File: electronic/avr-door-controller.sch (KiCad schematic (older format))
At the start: 74 parts, among them CON1 24V, J1 DOOR1, J2 DOOR2, P1 Digital, P10 DOOR2 BTN, P2 Analog, P3 DOOR1 BTN, P6 USB_A, P7 CLOCK, Q1 Q_NPN_EBC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

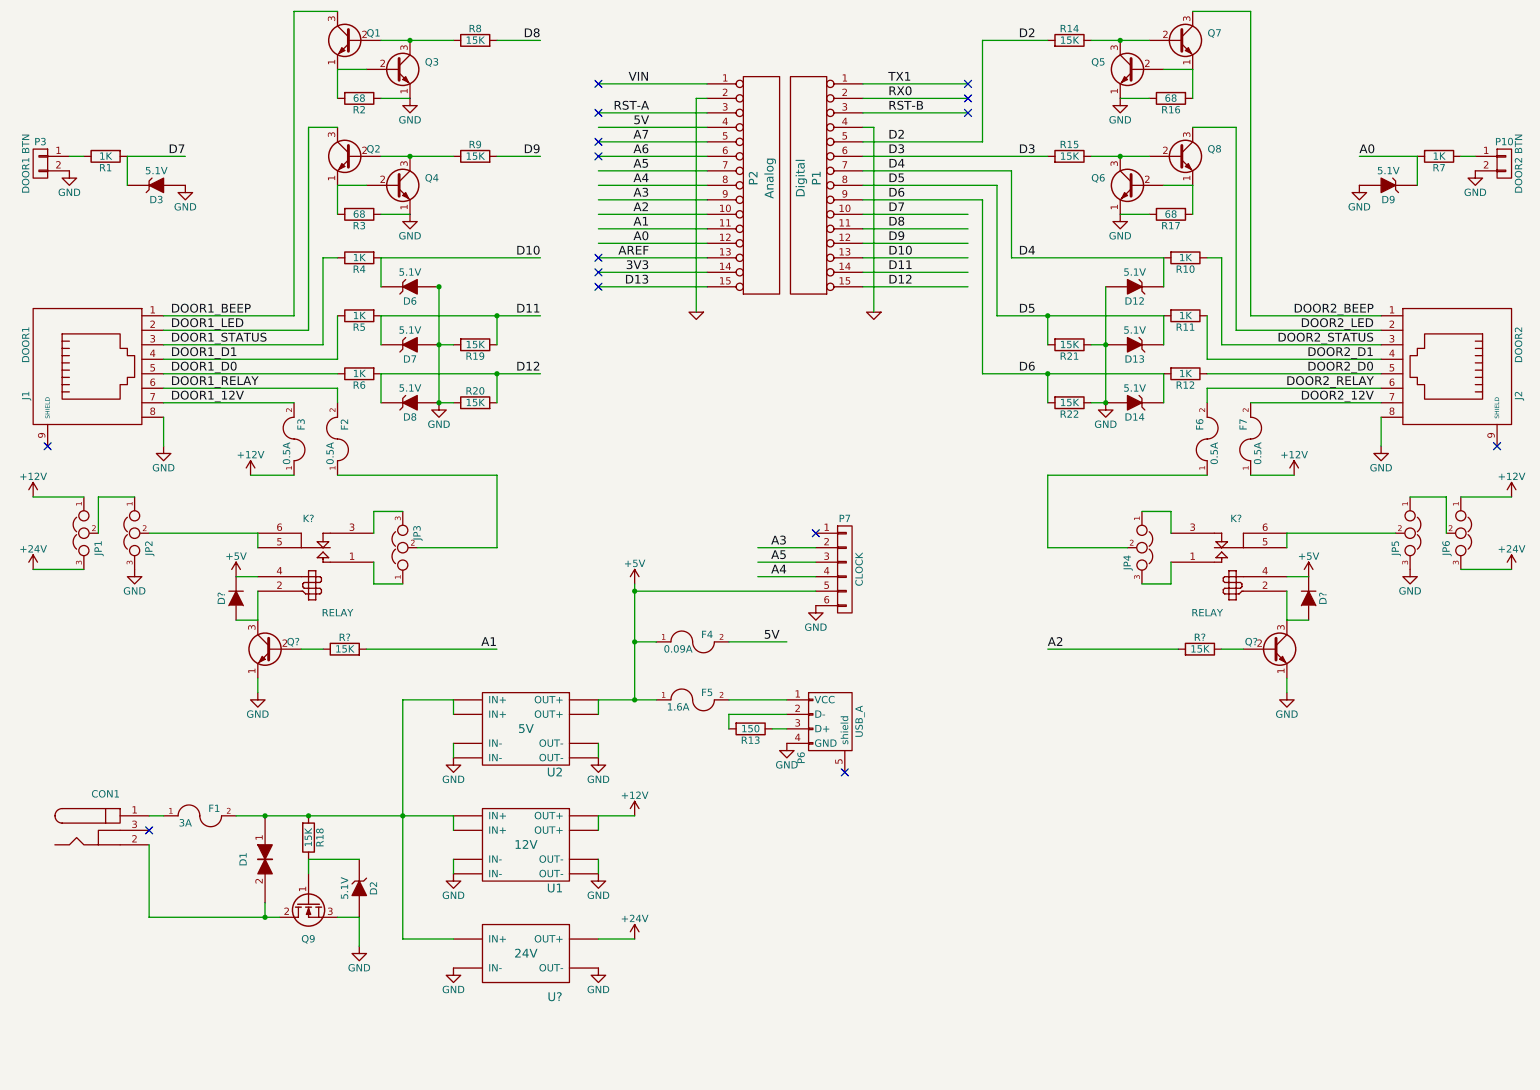
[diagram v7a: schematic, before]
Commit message: electronic: schematics: Annotate the new components
Signed-off-by: Alban Bedel <albeu@free.fr>
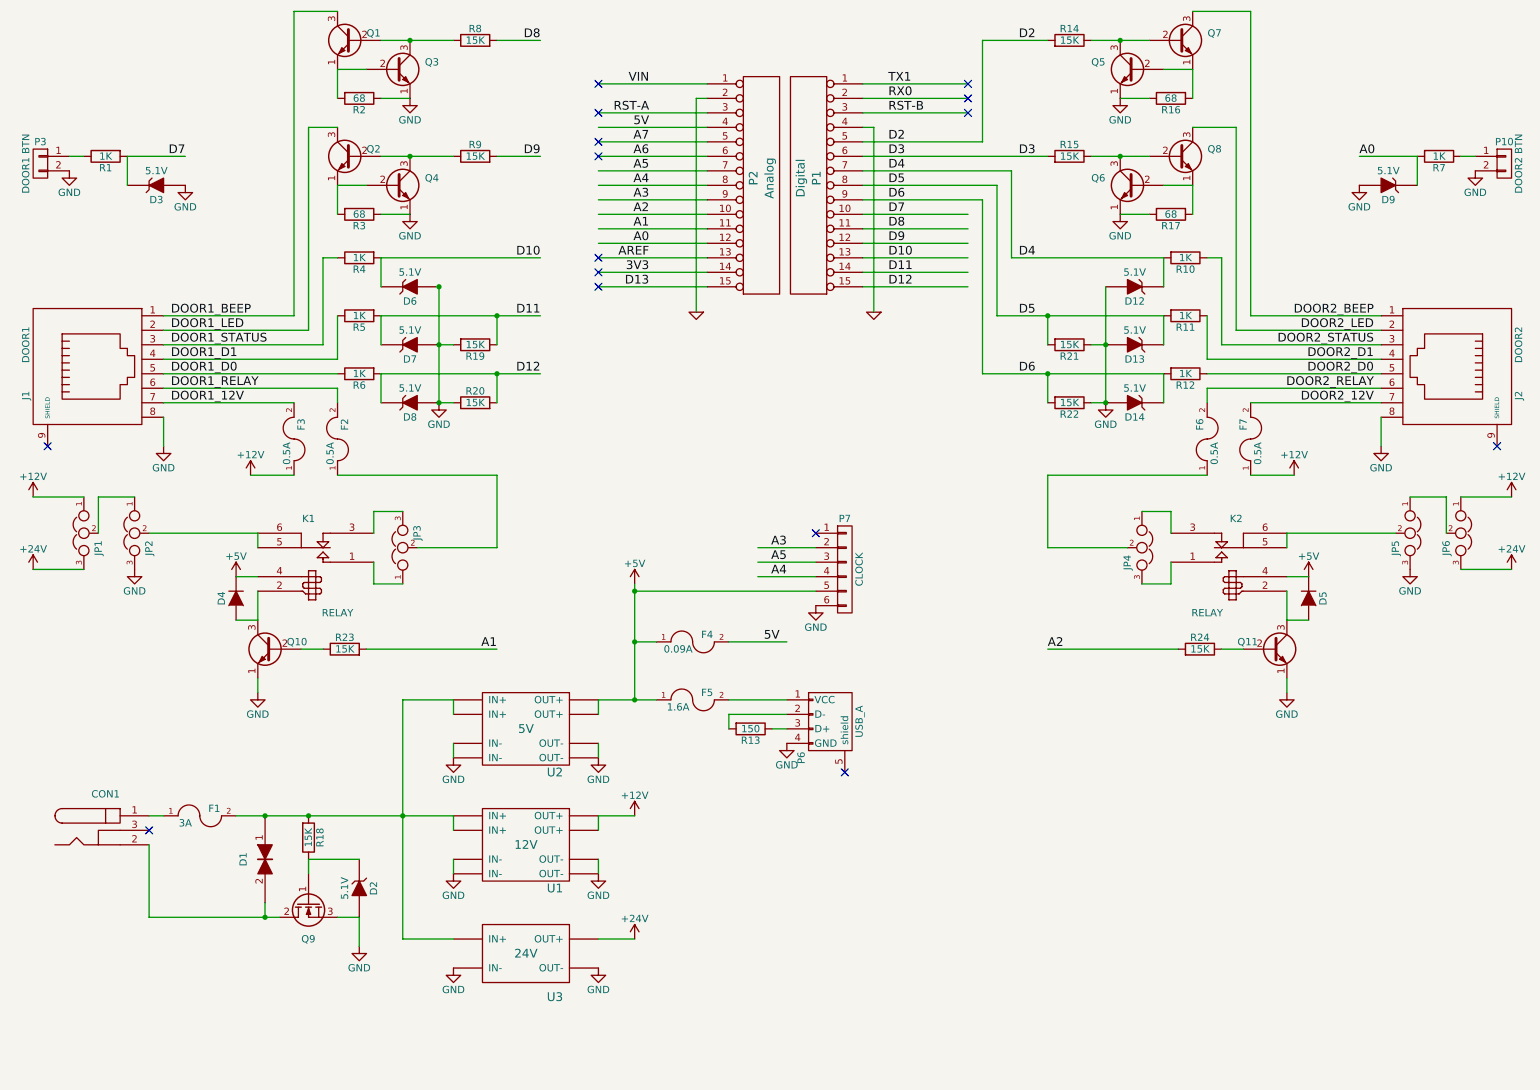
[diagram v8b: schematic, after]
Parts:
- gave numbers to parts that had none: 9
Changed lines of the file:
@@
 RX0
 $Comp
-L GND-RESCUE-avr-door-controller #PWR24
+L GND-RESCUE-avr-door-controller #PWR26
 U 1 1 551D979C
 P 6600 2975
-F 0 "#PWR24" H 6600 2975 30  0001 C CNN
+F 0 "#PWR26" H 6600 2975 30  0001 C CNN
 F 1 "GND" H 6600 2905 30  0001 C CNN
 F 2 "" H 6600 2975 60  0000 C CNN
@@
 AREF
 $Comp
-L GND-RESCUE-avr-door-controller #PWR21
+L GND-RESCUE-avr-door-controller #PWR23
 U 1 1 551D9FD7
 P 5375 2975
-F 0 "#PWR21" H 5375 2975 30  0001 C CNN
+F 0 "#PWR23" H 5375 2975 30  0001 C CNN
 F 1 "GND" H 5375 2905 30  0001 C CNN
 F 2 "" H 5375 2975 60  0000 C CNN
@@
 $EndComp
 $Comp
-L GND #PWR7
+L GND #PWR10
 U 1 1 58EE059F
 P 3050 7350
-F 0 "#PWR7" H 3050 7100 50  0001 C CNN
+F 0 "#PWR10" H 3050 7100 50  0001 C CNN
 F 1 "GND" H 3050 7200 50  0000 C CNN
 F 2 "" H 3050 7350 50  0000 C CNN
@@
 $EndComp
 $Comp
-L GND #PWR14
+L GND #PWR15
 U 1 1 58EE0CDC
 P 3700 6850
-F 0 "#PWR14" H 3700 6600 50  0001 C CNN
+F 0 "#PWR15" H 3700 6600 50  0001 C CNN
 F 1 "GND" H 3700 6700 50  0000 C CNN
 F 2 "" H 3700 6850 50  0000 C CNN
@@
 $EndComp
 $Comp
-L GND #PWR13
+L GND #PWR14
 U 1 1 58EE0D1B
 P 3700 6050
-F 0 "#PWR13" H 3700 5800 50  0001 C CNN
+F 0 "#PWR14" H 3700 5800 50  0001 C CNN
 F 1 "GND" H 3700 5900 50  0000 C CNN
 F 2 "" H 3700 6050 50  0000 C CNN
@@
 $EndComp
 $Comp
-L GND #PWR15
+L GND #PWR13
 U 1 1 58EE5748
 P 3600 3600
-F 0 "#PWR15" H 3600 3350 50  0001 C CNN
+F 0 "#PWR13" H 3600 3350 50  0001 C CNN
 F 1 "GND" H 3600 3450 50  0000 C CNN
 F 2 "" H 3600 3600 50  0000 C CNN
@@
 DOOR1_12V
 $Comp
-L +12V #PWR16
+L +12V #PWR8
 U 1 1 58EE7D92
 P 2300 4100
-F 0 "#PWR16" H 2300 3950 50  0001 C CNN
+F 0 "#PWR8" H 2300 3950 50  0001 C CNN
 F 1 "+12V" H 2300 4240 50  0000 C CNN
 F 2 "" H 2300 4100 50  0000 C CNN
@@
 NoConn ~ 10900 3900
 $Comp
-L GND #PWR32
+L GND #PWR34
 U 1 1 58EF639B
 P 10100 3900
-F 0 "#PWR32" H 10100 3650 50  0001 C CNN
+F 0 "#PWR34" H 10100 3650 50  0001 C CNN
 F 1 "GND" H 10100 3750 50  0000 C CNN
 F 2 "" H 10100 3900 50  0000 C CNN
@@
 $EndComp
 $Comp
-L GND #PWR26
+L GND #PWR27
 U 1 1 58EF63EA
 P 8200 3600
-F 0 "#PWR26" H 8200 3350 50  0001 C CNN
+F 0 "#PWR27" H 8200 3350 50  0001 C CNN
 F 1 "GND" H 8200 3450 50  0000 C CNN
 F 2 "" H 8200 3600 50  0000 C CNN
@@
 DOOR2_12V
 $Comp
-L +12V #PWR25
+L +12V #PWR31
 U 1 1 58EF6431
 P 9500 4100
-F 0 "#PWR25" H 9500 3950 50  0001 C CNN
+F 0 "#PWR31" H 9500 3950 50  0001 C CNN
 F 1 "+12V" H 9500 4240 50  0000 C CNN
 F 2 "" H 9500 4100 50  0000 C CNN
@@
 $EndComp
 $Comp
-L GND #PWR33
+L GND #PWR35
 U 1 1 58EF6459
 P 10300 4750
-F 0 "#PWR33" H 10300 4500 50  0001 C CNN
+F 0 "#PWR35" H 10300 4500 50  0001 C CNN
 F 1 "GND" H 10300 4600 50  0000 C CNN
 F 2 "" H 10300 4750 50  0000 C CNN
@@
 $EndComp
 $Comp
-L +12V #PWR35
+L +12V #PWR37
 U 1 1 58EF6465
 P 11000 4250
-F 0 "#PWR35" H 11000 4100 50  0001 C CNN
+F 0 "#PWR37" H 11000 4100 50  0001 C CNN
 F 1 "+12V" H 11000 4390 50  0000 C CNN
 F 2 "" H 11000 4250 50  0000 C CNN
@@
 A0
 $Comp
-L GND #PWR34
+L GND #PWR36
 U 1 1 58EF64A2
 P 10750 2000
-F 0 "#PWR34" H 10750 1750 50  0001 C CNN
+F 0 "#PWR36" H 10750 1750 50  0001 C CNN
 F 1 "GND" H 10750 1850 50  0000 C CNN
 F 2 "" H 10750 2000 50  0000 C CNN
@@
 5V
 $Comp
-L +12V #PWR20
+L +12V #PWR21
 U 1 1 58EFEBD6
 P 4950 6450
-F 0 "#PWR20" H 4950 6300 50  0001 C CNN
+F 0 "#PWR21" H 4950 6300 50  0001 C CNN
 F 1 "+12V" H 4950 6590 50  0000 C CNN
 F 2 "" H 4950 6450 50  0000 C CNN
@@
 $EndComp
 $Comp
-L +5V #PWR19
+L +5V #PWR20
 U 1 1 58EF6BAF
 P 4950 4850
-F 0 "#PWR19" H 4950 4700 50  0001 C CNN
+F 0 "#PWR20" H 4950 4700 50  0001 C CNN
 F 1 "+5V" H 4950 4990 50  0000 C CNN
 F 2 "" H 4950 4850 50  0000 C CNN
@@
 5V
 $Comp
-L GND #PWR22
+L GND #PWR24
 U 1 1 58F1DEA9
 P 6000 5950
-F 0 "#PWR22" H 6000 5700 50  0001 C CNN
+F 0 "#PWR24" H 6000 5700 50  0001 C CNN
 F 1 "GND" H 6000 5800 50  0000 C CNN
 F 2 "" H 6000 5950 50  0000 C CNN
@@
 $EndComp
 $Comp
-L GND #PWR23
+L GND #PWR25
 U 1 1 58F2A167
 P 6200 5000
-F 0 "#PWR23" H 6200 4750 50  0001 C CNN
+F 0 "#PWR25" H 6200 4750 50  0001 C CNN
 F 1 "GND" H 6200 4850 50  0000 C CNN
 F 2 "" H 6200 5000 50  0000 C CNN
@@
 $EndComp
 $Comp
-L GND #PWR27
+L GND #PWR28
 U 1 1 59810EAD
 P 8300 1500
-F 0 "#PWR27" H 8300 1250 50  0001 C CNN
+F 0 "#PWR28" H 8300 1250 50  0001 C CNN
 F 1 "GND" H 8300 1350 50  0000 C CNN
 F 2 "" H 8300 1500 50  0000 C CNN
@@
 $EndComp
 $Comp
-L GND #PWR31
+L GND #PWR33
 U 1 1 59814C5D
 P 9950 2100
-F 0 "#PWR31" H 9950 1850 50  0001 C CNN
+F 0 "#PWR33" H 9950 1850 50  0001 C CNN
 F 1 "GND" H 9950 1950 50  0000 C CNN
 F 2 "" H 9950 2100 50  0000 C CNN
@@
 $EndComp
 $Comp
-L GND #PWR28
+L GND #PWR29
 U 1 1 598278C9
 P 8300 2300
-F 0 "#PWR28" H 8300 2050 50  0001 C CNN
+F 0 "#PWR29" H 8300 2050 50  0001 C CNN
 F 1 "GND" H 8300 2150 50  0000 C CNN
 F 2 "" H 8300 2300 50  0000 C CNN
@@
 $EndComp
 $Comp
-L +24V #PWR36
+L +24V #PWR38
 U 1 1 58F223E9
 P 11000 4750
-F 0 "#PWR36" H 11000 4600 50  0001 C CNN
+F 0 "#PWR38" H 11000 4600 50  0001 C CNN
 F 1 "+24V" H 11000 4890 50  0000 C CNN
 F 2 "" H 11000 4750 50  0000 C CNN
@@
 	3700 5650 3350 5650
 $Comp
-L RELAY K?
+L RELAY K1
 U 1 1 59BD92DD
 P 2750 4700
-F 0 "K?" H 2700 5000 50  0000 C CNN
+F 0 "K1" H 2700 5000 50  0000 C CNN
 F 1 "RELAY" H 2900 4350 50  0000 C CNN
 F 2 "" H 2750 4850 50  0000 C CNN
@@
 	4000 4600 3450 4600
 $Comp
-L Q_NPN_EBC Q?
+L Q_NPN_EBC Q10
 U 1 1 59BDCFE1
 P 2450 5300
-F 0 "Q?" H 2350 5350 50  0000 R CNN
+F 0 "Q10" H 2350 5350 50  0000 R CNN
 F 1 "Q_NPN_EBC" H 3050 5250 50  0001 R CNN
 F 2 "TO_SOT_Packages_THT:TO-92_Inline_Narrow_Oval" H 2650 5400 50  0001 C CNN
@@
 	2350 5600 2350 5500
 $Comp
-L R R?
+L R R23
 U 1 1 59BDDD33
 P 2950 5300
-F 0 "R?" V 3030 5300 50  0000 C CNN
+F 0 "R23" V 3030 5300 50  0000 C CNN
 F 1 "15K" V 2950 5300 50  0000 C CNN
 F 2 "Resistors_ThroughHole:Resistor_Horizontal_RM10mm" V 2880 5300 50  0001 C CNN
@@
 	2350 4500 2350 4600
 $Comp
-L +5V #PWR?
+L +5V #PWR7
 U 1 1 59BDEE33
 P 2200 4800
-F 0 "#PWR?" H 2200 4650 50  0001 C CNN
+F 0 "#PWR7" H 2200 4650 50  0001 C CNN
 F 1 "+5V" H 2200 4940 50  0000 C CNN
 F 2 "" H 2200 4800 50  0000 C CNN
@@
 	2200 4800 2350 4800
 $Comp
-L D D?
+L D D4
 U 1 1 59BE2ACA
 P 2200 4950
-F 0 "D?" H 2200 5050 50  0000 C CNN
+F 0 "D4" H 2200 5050 50  0000 C CNN
 F 1 "D" H 2200 4850 50  0001 C CNN
 F 2 "" H 2200 4950 50  0000 C CNN
@@
 	2350 5100 2200 5100
 $Comp
-L GND #PWR?
+L GND #PWR30
 U 1 1 59BF0A4D
 P 9450 5600
-F 0 "#PWR?" H 9450 5350 50  0001 C CNN
+F 0 "#PWR30" H 9450 5350 50  0001 C CNN
 F 1 "GND" H 9450 5450 50  0000 C CNN
 F 2 "" H 9450 5600 50  0000 C CNN
@@
 	8700 5300 7800 5300
 $Comp
-L RELAY K?
+L RELAY K2
 U 1 1 59BF0A5A
 P 9050 4700
-F 0 "K?" H 9000 5000 50  0000 C CNN
+F 0 "K2" H 9000 5000 50  0000 C CNN
 F 1 "RELAY" H 9200 4350 50  0000 C CNN
 F 2 "" H 9050 4850 50  0000 C CNN
@@
 	7800 4600 8350 4600
 $Comp
-L Q_NPN_EBC Q?
+L Q_NPN_EBC Q11
 U 1 1 59BF0A67
 P 9350 5300
-F 0 "Q?" H 9250 5350 50  0000 R CNN
+F 0 "Q11" H 9250 5350 50  0000 R CNN
 F 1 "Q_NPN_EBC" H 9950 5250 50  0001 R CNN
 F 2 "TO_SOT_Packages_THT:TO-92_Inline_Narrow_Oval" H 9550 5400 50  0001 C CNN
@@
 	9450 5600 9450 5500
 $Comp
-L R R?
+L R R24
 U 1 1 59BF0A70
 P 8850 5300
-F 0 "R?" V 8930 5300 50  0000 C CNN
+F 0 "R24" V 8930 5300 50  0000 C CNN
 F 1 "15K" V 8850 5300 50  0000 C CNN
 F 2 "Resistors_ThroughHole:Resistor_Horizontal_RM10mm" V 8780 5300 50  0001 C CNN
@@
 	9450 4500 9450 4600
 $Comp
-L +5V #PWR?
+L +5V #PWR32
 U 1 1 59BF0A79
 P 9600 4800
-F 0 "#PWR?" H 9600 4650 50  0001 C CNN
+F 0 "#PWR32" H 9600 4650 50  0001 C CNN
 F 1 "+5V" H 9600 4940 50  0000 C CNN
 F 2 "" H 9600 4800 50  0000 C CNN
@@
 	9450 4800 9600 4800
 $Comp
-L D D?
+L D D5
 U 1 1 59BF0A81
 P 9600 4950
-F 0 "D?" H 9600 5050 50  0000 C CNN
+F 0 "D5" H 9600 5050 50  0000 C CNN
 F 1 "D" H 9600 4850 50  0001 C CNN
 F 2 "" H 9600 4950 50  0000 C CNN
@@
 	7800 4100 7800 4600
 $Comp
-L MT3608 U?
+L MT3608 U3
 U 1 1 59BF6CF4
 P 4200 7400
-F 0 "U?" H 4400 7700 60  0000 C CNN
+F 0 "U3" H 4400 7700 60  0000 C CNN
 F 1 "24V" H 4200 7400 60  0000 C CNN
 F 2 "" H 4200 7400 60  0000 C CNN
@@
 $EndComp
 $Comp
-L +24V #PWR?
+L +24V #PWR22
 U 1 1 59BF6F6A
 P 4950 7300
-F 0 "#PWR?" H 4950 7150 50  0001 C CNN
+F 0 "#PWR22" H 4950 7150 50  0001 C CNN
 F 1 "+24V" H 4950 7440 50  0000 C CNN
 F 2 "" H 4950 7300 50  0000 C CNN
@@
 	4950 7300 4950 7300
 $Comp
-L GND #PWR?
+L GND #PWR19
 U 1 1 59BF724D
 P 4700 7500
-F 0 "#PWR?" H 4700 7250 50  0001 C CNN
+F 0 "#PWR19" H 4700 7250 50  0001 C CNN
 F 1 "GND" H 4700 7350 50  0000 C CNN
 F 2 "" H 4700 7500 50  0000 C CNN
@@
 $EndComp
 $Comp
-L GND #PWR?
+L GND #PWR16
 U 1 1 59BF7F5A
 P 3700 7500
-F 0 "#PWR?" H 3700 7250 50  0001 C CNN
+F 0 "#PWR16" H 3700 7250 50  0001 C CNN
 F 1 "GND" H 3700 7350 50  0000 C CNN
 F 2 "" H 3700 7500 50  0000 C CNN
